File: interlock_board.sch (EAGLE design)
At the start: 6 parts, among them X1 1-227161-0

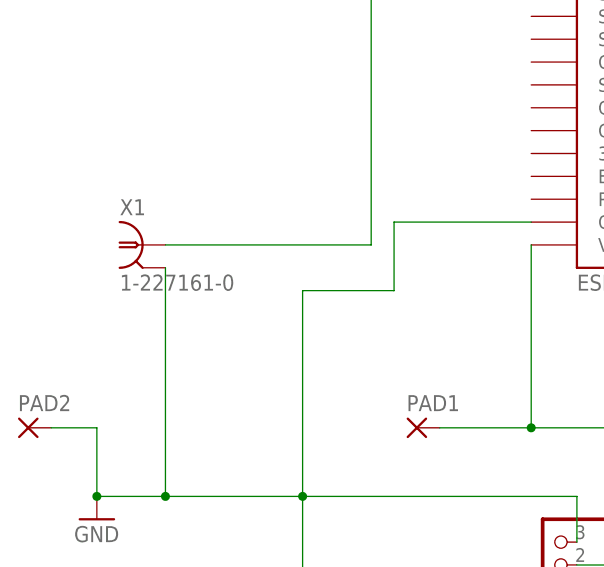
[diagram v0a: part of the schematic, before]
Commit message: Update with Alessandro's help
This update increases the copper trace size from 0.008" to 0.024" and moves them to the bottom layer, uses an updated BNC connector footprint (from JQI library) for better mechanical stability, and increased some hole sizes from 800 micron to 0.04".
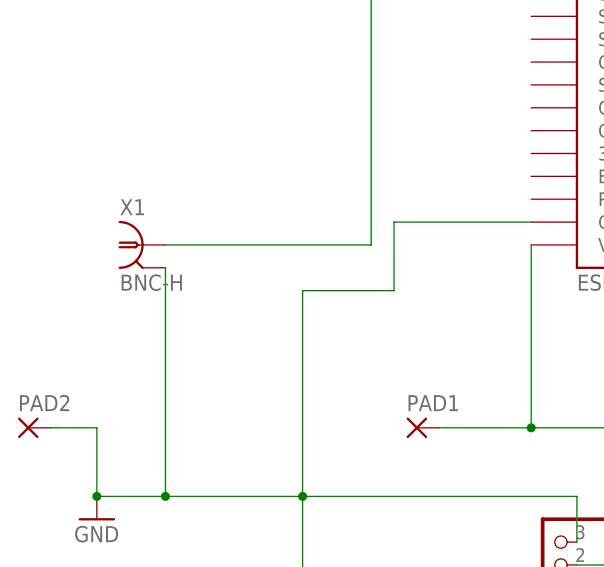
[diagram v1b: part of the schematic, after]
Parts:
- U$2: device ESP12E_DEVKIT:ESP12E_DEVKIT -> interlock_board:ESP12E_DEVKIT
- X1: value 1-227161-0 -> BNC-H; device con-coax:1-227161-0 -> connector-jqi:BNC-H
